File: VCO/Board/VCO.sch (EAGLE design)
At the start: 49 parts, among them IC1 TL074P, IC2 AD711N, T1 BC337, T2 BC337, X1 1503_02, X2 1503_02, X3 1503_02, X4 1503_02, X5 1503_02, X6 1503_02

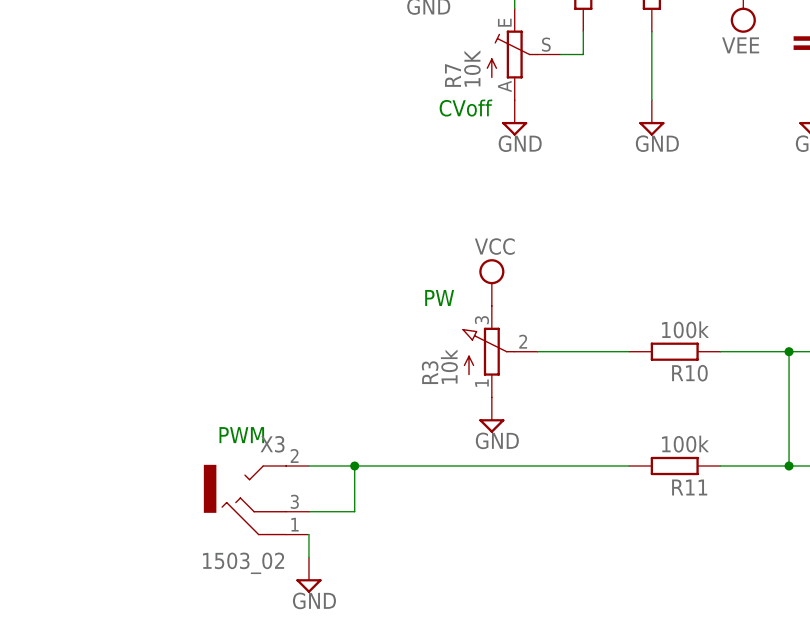
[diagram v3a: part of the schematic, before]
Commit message: Add PWM pot
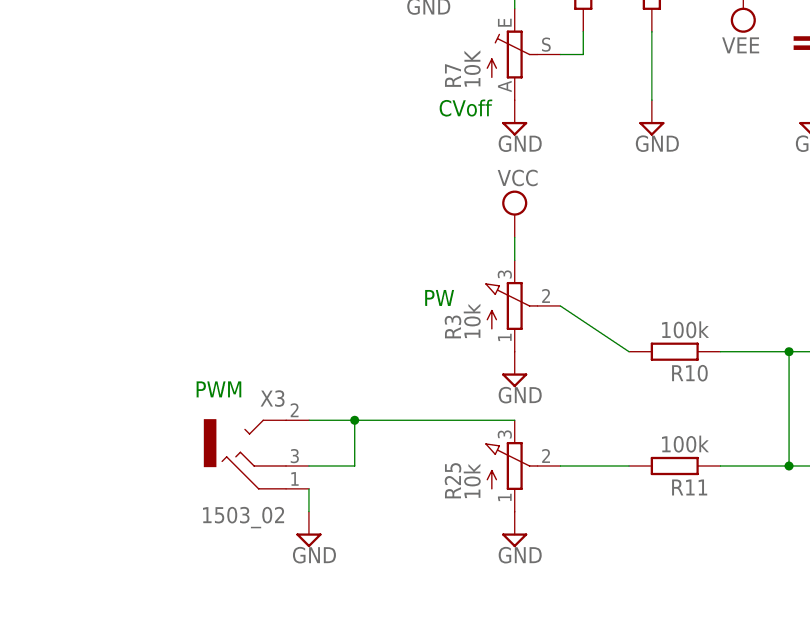
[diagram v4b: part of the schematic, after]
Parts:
- added R25: 10k, pot:3RP/1610N
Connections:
- new net N$16: R11.2, R25.S
- net GND: now also R25.A
- net N$28: now also R25.E; no longer R11.2
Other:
- moved on the sheet: R3, X3
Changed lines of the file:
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@@
 <part name="R19" library="pot" deviceset="TRIM_EU-" device="CA6V" value="10K"/>
 <part name="R21" library="pot" deviceset="TRIM_EU-" device="CA6V" value="10K"/>
+<part name="R25" library="pot" deviceset="3RP/1610N" device="" value="10k"/>
+<part name="SUPPLY37" library="supply2" deviceset="GND" device=""/>
 </parts>
 <sheets>
@@
 <text x="119.38" y="2.54" size="1.778" layer="91">SAW</text>
 <text x="121.92" y="-17.78" size="1.778" layer="91">PULSE</text>
-<text x="-53.34" y="-22.86" size="1.778" layer="91">PWM</text>
+<text x="-55.88" y="-17.78" size="1.778" layer="91">PWM</text>
 <text x="-30.48" y="-7.62" size="1.778" layer="91">PW</text>
 <text x="119.38" y="93.98" size="1.778" layer="91">SYNC</text>
@@
 <instance part="X5" gate="G$1" x="114.3" y="-2.54"/>
 <instance part="SUPPLY34" gate="GND" x="109.22" y="-12.7"/>
-<instance part="X3" gate="G$1" x="-48.26" y="-27.94" rot="MR0"/>
-<instance part="SUPPLY6" gate="GND" x="-43.18" y="-38.1"/>
-<instance part="R3" gate="G$1" x="-22.86" y="-12.7"/>
-<instance part="SUPPLY11" gate="GND" x="-22.86" y="-20.32"/>
-<instance part="SUPPLY10" gate="G$1" x="-22.86" y="-5.08" smashed="yes">
-<attribute name="VALUE" x="-24.765" y="-1.905" size="1.778" layer="96"/>
+<instance part="X3" gate="G$1" x="-48.26" y="-22.86" rot="MR0"/>
+<instance part="SUPPLY6" gate="GND" x="-43.18" y="-33.02"/>
+<instance part="R3" gate="G$1" x="-20.32" y="-7.62"/>
+<instance part="SUPPLY11" gate="GND" x="-20.32" y="-15.24"/>
+<instance part="SUPPLY10" gate="G$1" x="-20.32" y="2.54" smashed="yes">
+<attribute name="VALUE" x="-22.225" y="5.715" size="1.778" layer="96"/>
 </instance>
 <instance part="X4" gate="G$1" x="114.3" y="88.9"/>
@@
 <instance part="R19" gate="1" x="88.9" y="-20.32"/>
 <instance part="R21" gate="1" x="93.98" y="20.32"/>
+<instance part="R25" gate="G$1" x="-20.32" y="-25.4"/>
+<instance part="SUPPLY37" gate="GND" x="-20.32" y="-33.02"/>
 </instances>
 <busses>
@@
 <pinref part="X3" gate="G$1" pin="1"/>
 <pinref part="SUPPLY6" gate="GND" pin="GND"/>
-<wire x1="-43.18" y1="-33.02" x2="-43.18" y2="-35.56" width="0.1524" layer="91"/>
+<wire x1="-43.18" y1="-27.94" x2="-43.18" y2="-30.48" width="0.1524" layer="91"/>
 </segment>
 <segment>
@@
 <pinref part="SUPPLY30" gate="GND" pin="GND"/>
 <pinref part="R21" gate="1" pin="A"/>
+</segment>
+<segment>
+<pinref part="R25" gate="G$1" pin="A"/>
+<pinref part="SUPPLY37" gate="GND" pin="GND"/>
 </segment>
 </net>
@@
 <pinref part="R3" gate="G$1" pin="E"/>
 <pinref part="SUPPLY10" gate="G$1" pin="VCC"/>
+<wire x1="-20.32" y1="0" x2="-20.32" y2="-2.54" width="0.1524" layer="91"/>
 </segment>
 </net>
@@
 <segment>
 <pinref part="R10" gate="G$1" pin="2"/>
-<wire x1="-17.78" y1="-12.7" x2="-7.62" y2="-12.7" width="0.1524" layer="91"/>
+<wire x1="-15.24" y1="-7.62" x2="-7.62" y2="-12.7" width="0.1524" layer="91"/>
 <pinref part="R3" gate="G$1" pin="S"/>
 </segment>
@@
 <net name="N$28" class="0">
 <segment>
-<pinref part="R11" gate="G$1" pin="2"/>
-<wire x1="-43.18" y1="-25.4" x2="-38.1" y2="-25.4" width="0.1524" layer="91"/>
+<wire x1="-43.18" y1="-20.32" x2="-38.1" y2="-20.32" width="0.1524" layer="91"/>
 <pinref part="X3" gate="G$1" pin="2"/>
 <pinref part="X3" gate="G$1" pin="3"/>
-<wire x1="-43.18" y1="-30.48" x2="-38.1" y2="-30.48" width="0.1524" layer="91"/>
-<wire x1="-38.1" y1="-30.48" x2="-38.1" y2="-25.4" width="0.1524" layer="91"/>
-<junction x="-38.1" y="-25.4"/>
-<wire x1="-7.62" y1="-25.4" x2="-38.1" y2="-25.4" width="0.1524" layer="91"/>
+<wire x1="-43.18" y1="-25.4" x2="-38.1" y2="-25.4" width="0.1524" layer="91"/>
+<wire x1="-38.1" y1="-25.4" x2="-38.1" y2="-20.32" width="0.1524" layer="91"/>
+<pinref part="R25" gate="G$1" pin="E"/>
+<wire x1="-38.1" y1="-20.32" x2="-20.32" y2="-20.32" width="0.1524" layer="91"/>
+<junction x="-38.1" y="-20.32"/>
 </segment>
 </net>
@@
 </segment>
 </net>
+<net name="N$16" class="0">
+<segment>
+<pinref part="R11" gate="G$1" pin="2"/>
+<pinref part="R25" gate="G$1" pin="S"/>
+<wire x1="-7.62" y1="-25.4" x2="-15.24" y2="-25.4" width="0.1524" layer="91"/>
+</segment>
+</net>
